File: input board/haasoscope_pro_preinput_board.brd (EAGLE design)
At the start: 75 x 50 mm, 20 parts, among them J1 MOLEX_BNC_73100-0105, J4 8pin, K1 AQY21SOP

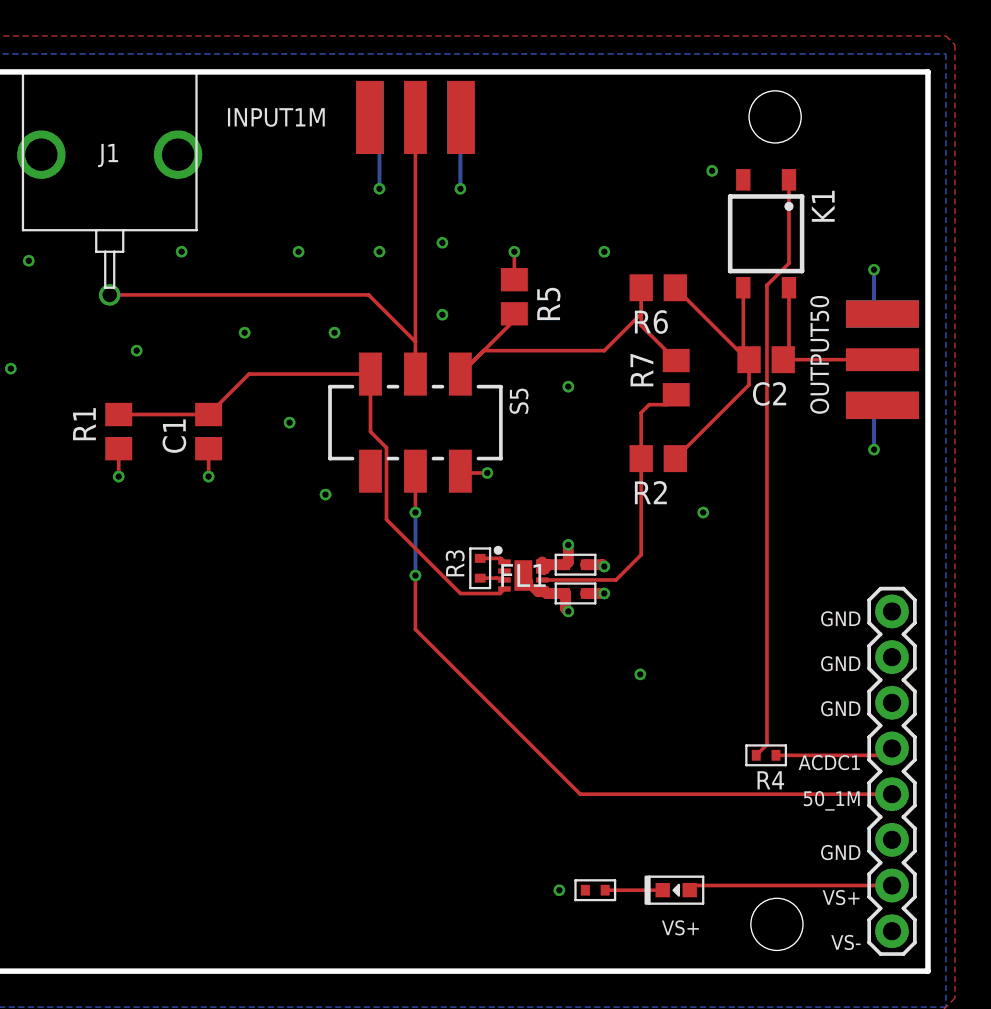
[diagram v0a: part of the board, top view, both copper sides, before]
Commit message: use rf relay instead of switch
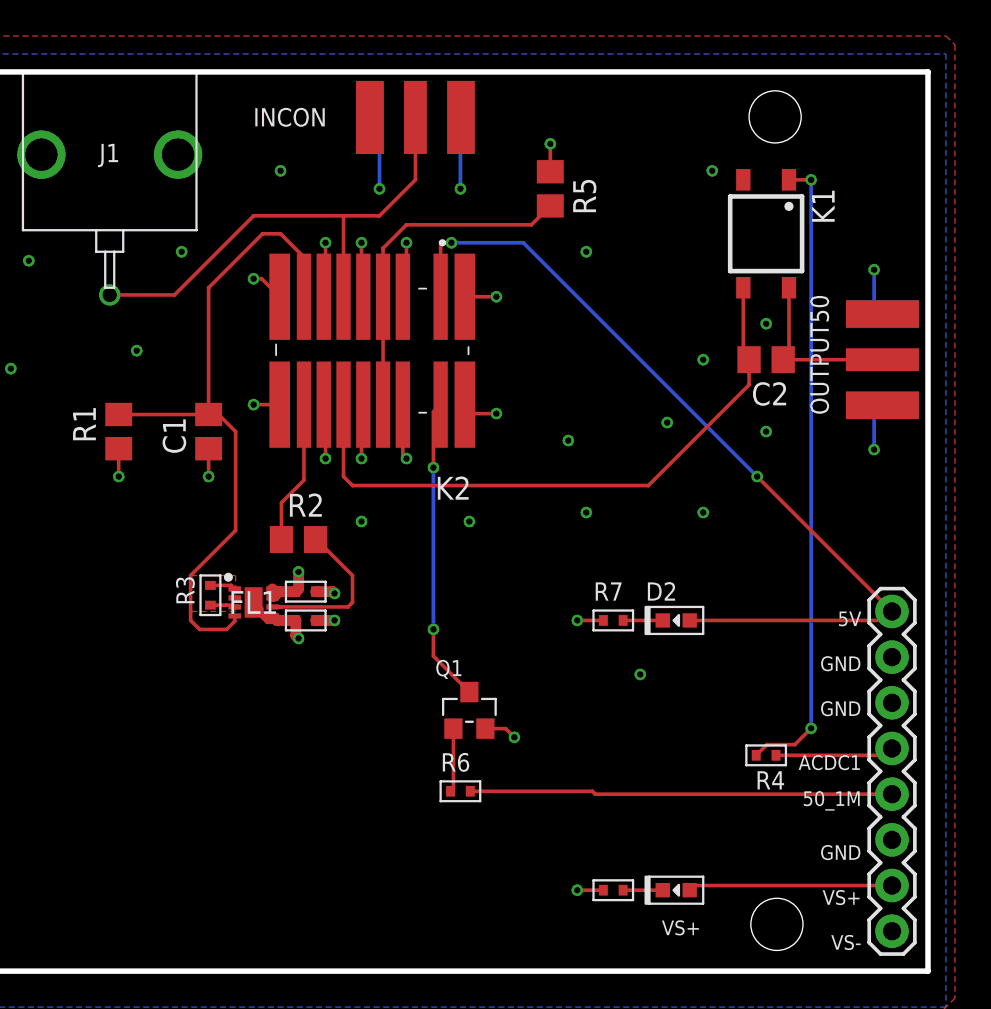
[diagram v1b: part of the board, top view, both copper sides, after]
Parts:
- removed S5: JS202011SCQN, switch-ck:JS202011SCQN
- added D2: green, MF_LEDs:LED0603
- added K2: G6K-2F-RF-T-TR03_DC5, G6K-2F-RF-T-TR03_DC5:G6K2FRFTTR03DC5
- added Q1: S8050, Seeed-Transistor:SOT-23
- INCON: value in1M -> in
- R6, R7: value 47 -> 1k; device resistor:R0805 -> MF_Passives:R0402
- moved R6 30.1 mm to (59.0, 10.0), turned to 0 degrees
- moved R2 20.5 mm to (50.0, 24.0), turned to 0 degrees
- moved C11 15.1 mm to (50.4, 21.1)
- moved C12 15.1 mm to (50.4, 19.5)
- moved FL1 15.1 mm to (47.5, 20.5)
- moved R3 15.1 mm to (45.1, 20.9)
- moved R7 13.9 mm to (67.5, 19.5), turned to 0 degrees
- moved R5 6.32 mm to (64.0, 43.5)
- moved R12 1.00 mm to (67.5, 4.50)
- renumbered INPUT1M to INCON
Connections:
- removed net N$10: C1.2, FL1.4, R1.2, S5.3
- removed net N$13: R5.2, R6.2, R7.2, S5.1
- removed net N$8: C2.2, K1.3, R2.1, R6.1
- new net 1MPATH: C1.2, FL1.4, K2.4, R1.2
- new net 1MPATH50: K2.5, R2.1
- new net 50PATH: K2.2, K2.7, R5.2
- new net 5V: D2.ANODE, J4.1, K2.1
- new net COIL1-: K2.8, Q1.3
- new net INPATH: INCON.P, J1.SIGNAL, K2.3
- new net N$7: D2.CATHODE, R7.P$2
- new net OUTPATH: C2.2, K1.3, K2.6
- net 50_1M: now also R6.P$2; no longer S5.5
- net GND: now also K2.MP1, K2.MP10, K2.MP2, K2.MP3, K2.MP4, K2.MP5, K2.MP6, K2.MP7, K2.MP8, K2.MP9, Q1.2, R7.P$1; no longer J4.1, S5.6
- net N$4: no longer R7.1
- net N$6: now also Q1.1, R6.P$1; no longer INCON.P, J1.SIGNAL, S5.2
- net VS+: no longer S5.4
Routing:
- net 5V: track 0.00 -> 48.0 mm, vias 0 -> 2
- net 1MPATH: track 0.00 -> 38.1 mm
- net OUTPATH: track 0.00 -> 35.1 mm
- net N$10: track 31.8 -> 0.00 mm
- net GND: track 20.3 -> 50.5 mm, vias 27 -> 39
- net N$6: track 32.3 -> 3.55 mm
- net INPATH: track 0.00 -> 27.6 mm
- net N$13: track 20.9 -> 0.00 mm
- net 50PATH: track 0.00 -> 20.5 mm
- net N$8: track 18.0 -> 0.00 mm
- net COIL1-: track 0.00 -> 17.0 mm, vias 0 -> 2
- net 50_1M: track 39.1 -> 23.5 mm, vias 2 -> 0
- net 1MPATH50: track 0.00 -> 8.37 mm
- net N$4: track 16.3 -> 9.43 mm
- net N$11: track 32.8 -> 35.4 mm, vias 0 -> 2
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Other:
- board text added: "5V"

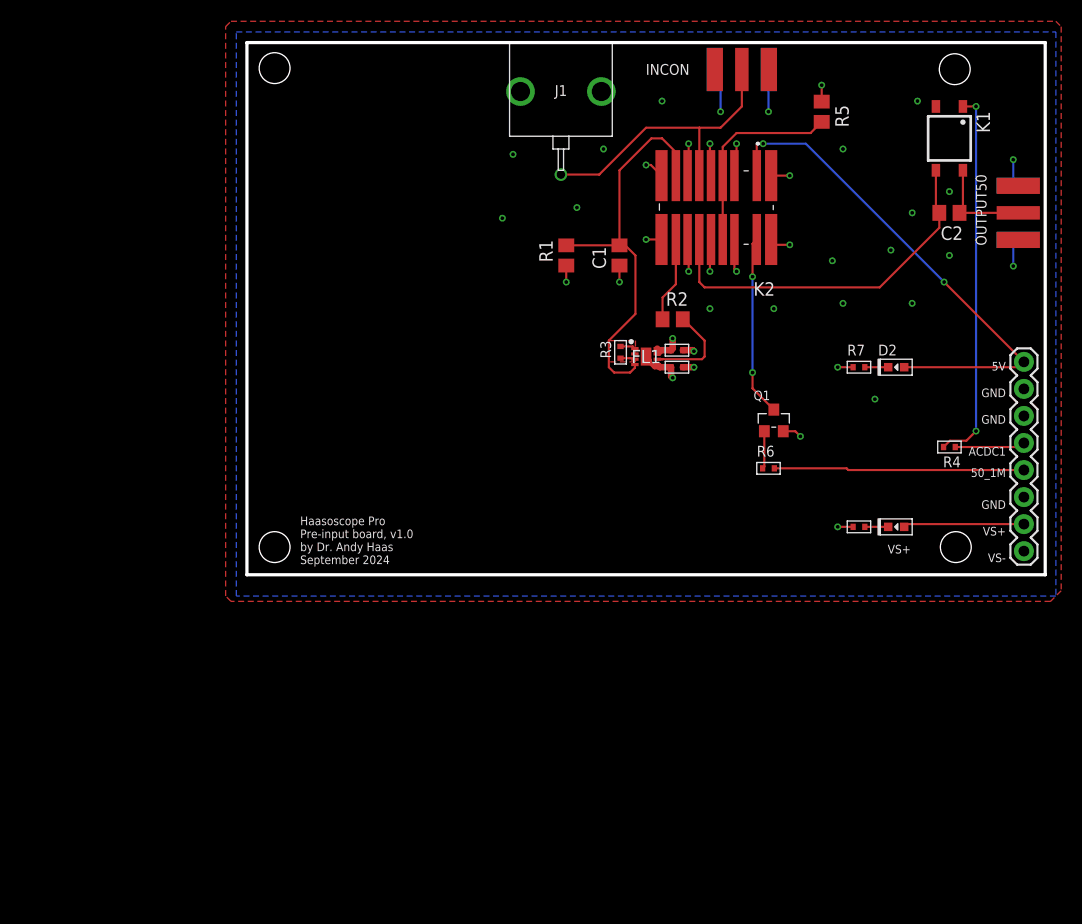
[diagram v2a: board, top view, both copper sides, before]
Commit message: add attenuator and fix relay footprint
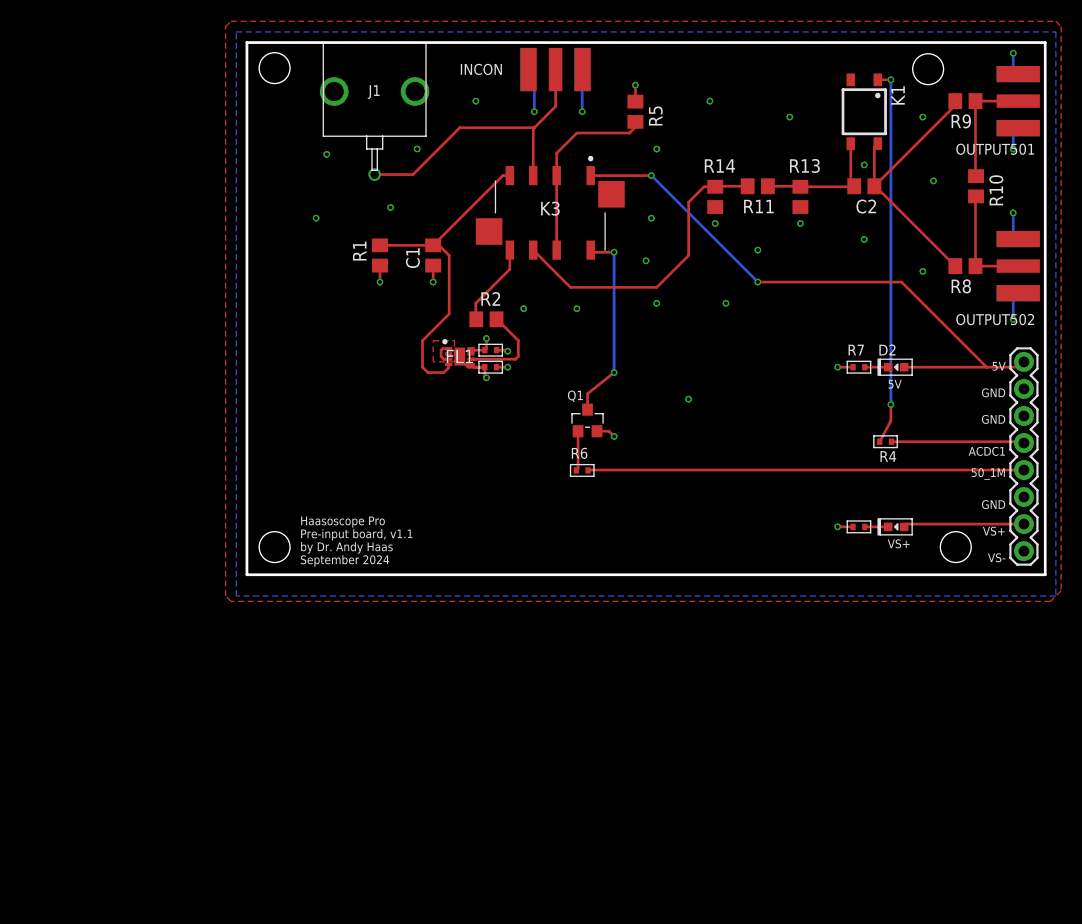
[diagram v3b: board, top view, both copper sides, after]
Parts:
- removed K2: G6K-2F-RF-T-TR03_DC5, G6K-2F-RF-T-TR03_DC5:G6K2FRFTTR03DC5
- removed OUTPUT50: out50, adafruit:SMA_EDGELAUNCH
- removed R3: 0, MF_Passives:R0402
- added K3: G6K-2F-RF-DC3, G6K-2F-RF-DC3:G6K2FRFDC3
- added OUTPUT501, OUTPUT502: out50, adafruit:SMA_EDGELAUNCH
- added R10, R8, R9: 47, resistor:R0805
- added R11: 120, resistor:R0805
- added R13, R14: 75, resistor:R0805
- R5: value 47 -> ?50?
- moved R6 17.5 mm to (41.5, 9.80)
- moved C1 17.5 mm to (27.5, 30.0)
- moved C11 17.5 mm to (32.9, 21.1)
- moved C12 17.5 mm to (32.9, 19.5)
- moved FL1 17.5 mm to (30.0, 20.5)
- moved INCON 17.5 mm to (39.0, 49.5)
- moved J1 17.5 mm to (22.0, 41.5)
- moved Q1 17.5 mm to (42.0, 14.5)
- moved R1 17.5 mm to (22.5, 30.0)
- moved R2 17.5 mm to (32.5, 24.0)
- moved R5 17.5 mm to (46.5, 43.5)
- moved C2 8.38 mm to (68.0, 36.5)
- moved K1 8.38 mm to (68.0, 43.5)
- moved R4 6.02 mm to (70.0, 12.5)
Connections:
- removed net N$2: FL1.3, R3.P$2
- removed net N$3: C2.1, K1.4, OUTPUT50.P
- new net N$10: OUTPUT501.P, R10.1, R9.1
- new net N$8: C2.1, K1.4, R8.2, R9.2
- new net N$9: OUTPUT502.P, R10.2, R8.1
- new net OUTPATHFILT: C2.2, K1.3, R11.1, R13.1
- net 1MPATH: now also K3.4; no longer K2.4
- net 1MPATH50: now also K3.5; no longer K2.5
- net 50PATH: now also K3.2, K3.7; no longer K2.2, K2.7
- net 5V: now also K3.1; no longer K2.1
- net COIL1-: now also K3.8; no longer K2.8
- net GND: now also K3.MP1, K3.MP2, OUTPUT501.GND@1, OUTPUT501.GND@2, OUTPUT501.GND@3, OUTPUT501.GND@4, OUTPUT502.GND@1, OUTPUT502.GND@2, OUTPUT502.GND@3, OUTPUT502.GND@4, R13.2, R14.2; no longer K2.MP1, K2.MP10, K2.MP2, K2.MP3, K2.MP4, K2.MP5, K2.MP6, K2.MP7, K2.MP8, K2.MP9, OUTPUT50.GND@1, OUTPUT50.GND@2, OUTPUT50.GND@3, OUTPUT50.GND@4
- net INPATH: now also K3.3; no longer K2.3
- net N$5: now also FL1.3; no longer R3.P$1
- net OUTPATH: now also K3.6, R11.2, R14.1; no longer C2.2, K1.3, K2.6
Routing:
- net N$8: track 0.00 -> 26.4 mm
- net GND: track 50.5 -> 29.6 mm, vias 39 -> 37
- net 50_1M: track 23.5 -> 41.0 mm
- net OUTPATHFILT: track 0.00 -> 12.8 mm
- net N$10: track 0.00 -> 12.0 mm
- net N$9: track 0.00 -> 11.1 mm
- net N$3: track 9.65 -> 0.00 mm
- net 5V: track 48.0 -> 56.1 mm
- net OUTPATH: track 35.1 -> 28.5 mm
- net 1MPATH: track 38.1 -> 31.5 mm
- net ACDC1: track 6.61 -> 12.5 mm
- net 50PATH: track 20.5 -> 18.4 mm
- net COIL1-: track 17.0 -> 18.4 mm
- net N$2: track 1.39 -> 0.00 mm
- net N$5: track 1.43 -> 2.19 mm
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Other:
- board text added: "Haasoscope Pro Pre-input board, v1.1 by Dr. Andy Haas September 2024"
- board text removed: "Haasoscope Pro Pre-input board, v1.0 by Dr. Andy Haas September 2024"

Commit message: add relay for attenuator
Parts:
- added K2: G6K-2F-RF-DC3, G6K-2F-RF-DC3:G6K2FRFDC3
- added Q2: S8050, Seeed-Transistor:SOT-23
- added R3: 1k, MF_Passives:R0402
- moved R11 10.6 mm to (54.5, 46.5)
- moved R14 9.86 mm to (49.0, 44.0)
- moved R13 9.01 mm to (59.0, 44.0)
- moved C1 6.50 mm to (21.0, 30.0)
- moved C11 6.50 mm to (26.4, 21.1)
- moved C12 6.50 mm to (26.4, 19.5)
- moved FL1 6.50 mm to (23.5, 20.5)
- moved INCON 6.50 mm to (32.5, 49.5)
- moved J1 6.50 mm to (15.5, 41.5)
- moved K3 6.50 mm to (32.0, 34.0)
- moved Q1 6.50 mm to (35.5, 14.5)
- moved R1 6.50 mm to (16.0, 30.0)
- moved R2 6.50 mm to (26.0, 24.0)
- moved R5 6.50 mm to (40.0, 43.5)
- moved R6 6.50 mm to (35.0, 9.80)
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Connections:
- new net ATT: J4.3, R3.P$2
- new net COIL2-: K2.8, Q2.3
- new net FILTIN: K2.4, R11.2, R14.1
- new net FILTOUT: K2.5, R11.1, R13.1
- new net N$2: Q2.1, R3.P$1
- new net NOFILT: K2.2, K2.7
- net 5V: now also K2.1
- net GND: now also K2.MP1, K2.MP2, Q2.2; no longer J4.3
- net OUTPATH: now also K2.3; no longer R11.2, R14.1
- net OUTPATHFILT: now also K2.6; no longer R11.1, R13.1
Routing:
- net ATT: track 0.00 -> 32.8 mm
- net COIL2-: track 0.00 -> 27.1 mm, vias 0 -> 2
- net FILTIN: track 0.00 -> 21.5 mm
- net 5V: track 56.1 -> 74.7 mm
- net FILTOUT: track 0.00 -> 12.0 mm
- net OUTPATHFILT: track 12.8 -> 21.8 mm
- net NOFILT: track 0.00 -> 7.00 mm
- net 50_1M: track 41.0 -> 47.5 mm
- net N$2: track 0.00 -> 6.13 mm
- net OUTPATH: track 28.5 -> 26.7 mm
- net N$11: track 35.5 -> 36.4 mm
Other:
- board text added: "ATT"
- board text added: "Haasoscope Pro Pre-input board, v1.11 by Dr. Andy Haas September 2024"
- board text removed: "Haasoscope Pro Pre-input board, v1.1 by Dr. Andy Haas September 2024"

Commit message: don't place 10pF, fix some labels
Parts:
- C1: value 10pF -> ?10pF?
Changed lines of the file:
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@@
 <element name="R1" library="resistor" library_urn="urn:adsk.eagle:library:348" package="R0805" package3d_urn="urn:adsk.eagle:package:23553/2" value="1M" x="16" y="30" smashed="yes" rot="R90">
 <attribute name="NAME" x="14.73" y="29.365" size="1.27" layer="25" rot="R90"/>
-<attribute name="VALUE" x="18.54" y="29.365" size="1.27" layer="27" rot="R90"/>
+<attribute name="VALUE" x="18.44" y="29.065" size="1.27" layer="21" rot="R90"/>
 </element>
-<element name="C1" library="resistor" library_urn="urn:adsk.eagle:library:348" package="C0805" package3d_urn="urn:adsk.eagle:package:23617/2" value="10pF" x="21" y="30" smashed="yes" rot="R90">
-<attribute name="NAME" x="19.73" y="28.73" size="1.27" layer="25" rot="R90"/>
-<attribute name="VALUE" x="23.54" y="28.73" size="1.27" layer="27" rot="R90"/>
+<element name="C1" library="resistor" library_urn="urn:adsk.eagle:library:348" package="C0805" package3d_urn="urn:adsk.eagle:package:23617/2" value="?10pF?" x="21" y="30" smashed="yes" rot="R90">
+<attribute name="NAME" x="19.83" y="29.13" size="1.27" layer="25" rot="R90"/>
+<attribute name="VALUE" x="23.54" y="27.73" size="1.27" layer="21" rot="R90"/>
 </element>
 <element name="R2" library="resistor" library_urn="urn:adsk.eagle:library:348" package="R0805" package3d_urn="urn:adsk.eagle:package:23553/2" value="47" x="26" y="24" smashed="yes">
 <attribute name="NAME" x="25.365" y="25.27" size="1.27" layer="25"/>
-<attribute name="VALUE" x="25.365" y="21.46" size="1.27" layer="27"/>
+<attribute name="VALUE" x="25.265" y="21.86" size="1.27" layer="21"/>
 </element>
 <element name="J1" library="connector" package="MOLEX-BNC-73100-0105" value="MOLEX_BNC_73100-0105" x="15.5" y="41.5" smashed="yes" rot="R180">
@@
 <element name="C2" library="resistor" library_urn="urn:adsk.eagle:library:348" package="C0805" package3d_urn="urn:adsk.eagle:package:23617/2" value="1uF" x="68" y="36.5" smashed="yes" rot="R180">
 <attribute name="NAME" x="69.27" y="35.23" size="1.27" layer="25" rot="R180"/>
-<attribute name="VALUE" x="69.27" y="39.04" size="1.27" layer="27" rot="R180"/>
+<attribute name="VALUE" x="69.27" y="39.04" size="1.27" layer="21" rot="R180"/>
 </element>
 <element name="R5" library="resistor" library_urn="urn:adsk.eagle:library:348" package="R0805" package3d_urn="urn:adsk.eagle:package:23553/2" value="?50?" x="40" y="43.5" smashed="yes" rot="R270">
 <attribute name="NAME" x="41.27" y="44.135" size="1.27" layer="25" rot="R270"/>
-<attribute name="VALUE" x="37.46" y="44.135" size="1.27" layer="27" rot="R270"/>
+<attribute name="VALUE" x="37.46" y="45.135" size="1.27" layer="21" rot="R270"/>
 </element>
 <element name="Q1" library="Seeed-Transistor" library_urn="urn:adsk.eagle:library:477" package="SOT-23" package3d_urn="urn:adsk.eagle:package:33015/1" value="S8050" x="35.5" y="14.5" smashed="yes">
@@
 <attribute name="MOUSER_PRICE-STOCK" value="https://www.mouser.co.uk/ProductDetail/Omron-Electronics/G6K-2F-RF-DC3?qs=Pjd0UV7BHP8BL6Nr%252BzW3GA%3D%3D" x="32" y="34" size="1.778" layer="27" rot="R180" display="off"/>
 <attribute name="NAME" x="32" y="34.4" size="1.27" layer="25" rot="R180" align="center"/>
-<attribute name="VALUE" x="32" y="27.9" size="1.27" layer="27" rot="R180" align="center"/>
+<attribute name="VALUE" x="32" y="27.9" size="1.27" layer="21" rot="R180" align="center"/>
 </element>
 <element name="OUTPUT501" library="adafruit" package="SMA_EDGELAUNCH" value="out50" x="84.5" y="44.5" smashed="yes" rot="R180">
@@
 <element name="R8" library="resistor" library_urn="urn:adsk.eagle:library:348" package="R0805" package3d_urn="urn:adsk.eagle:package:23553/2" value="47" x="77.5" y="29" smashed="yes" rot="R180">
 <attribute name="NAME" x="78.135" y="27.73" size="1.27" layer="25" rot="R180"/>
-<attribute name="VALUE" x="78.135" y="31.54" size="1.27" layer="27" rot="R180"/>
+<attribute name="VALUE" x="78.135" y="31.54" size="1.27" layer="21" rot="R180"/>
 </element>
 <element name="R9" library="resistor" library_urn="urn:adsk.eagle:library:348" package="R0805" package3d_urn="urn:adsk.eagle:package:23553/2" value="47" x="77.5" y="44.5" smashed="yes" rot="R180">
 <attribute name="NAME" x="78.135" y="43.23" size="1.27" layer="25" rot="R180"/>
-<attribute name="VALUE" x="78.135" y="47.04" size="1.27" layer="27" rot="R180"/>
+<attribute name="VALUE" x="78.135" y="47.04" size="1.27" layer="21" rot="R180"/>
 </element>
 <element name="R10" library="resistor" library_urn="urn:adsk.eagle:library:348" package="R0805" package3d_urn="urn:adsk.eagle:package:23553/2" value="47" x="78.5" y="36.5" smashed="yes" rot="R270">
 <attribute name="NAME" x="79.77" y="37.635" size="1.27" layer="25" rot="R270"/>
-<attribute name="VALUE" x="75.96" y="37.135" size="1.27" layer="27" rot="R270"/>
+<attribute name="VALUE" x="75.96" y="37.135" size="1.27" layer="21" rot="R270"/>
 </element>
 <element name="Q2" library="Seeed-Transistor" library_urn="urn:adsk.eagle:library:477" package="SOT-23" package3d_urn="urn:adsk.eagle:package:33015/1" value="S8050" x="47.5" y="14.5" smashed="yes">
@@
 <attribute name="MOUSER_PRICE-STOCK" value="https://www.mouser.co.uk/ProductDetail/Omron-Electronics/G6K-2F-RF-DC3?qs=Pjd0UV7BHP8BL6Nr%252BzW3GA%3D%3D" x="47" y="31.5" size="1.778" layer="27" display="off"/>
 <attribute name="NAME" x="52" y="34.6" size="1.27" layer="25" align="center"/>
-<attribute name="VALUE" x="52" y="28.1" size="1.27" layer="27" align="center"/>
+<attribute name="VALUE" x="52" y="28.1" size="1.27" layer="21" align="center"/>
 </element>
 <element name="R11" library="resistor" library_urn="urn:adsk.eagle:library:348" package="R0805" package3d_urn="urn:adsk.eagle:package:23553/2" value="120" x="54.5" y="46.5" smashed="yes" rot="R180">
 <attribute name="NAME" x="56.135" y="45.23" size="1.27" layer="25" rot="R180"/>
-<attribute name="VALUE" x="55.135" y="49.04" size="1.27" layer="27" rot="R180"/>
+<attribute name="VALUE" x="55.135" y="49.04" size="1.27" layer="21" rot="R180"/>
 </element>
 <element name="R13" library="resistor" library_urn="urn:adsk.eagle:library:348" package="R0805" package3d_urn="urn:adsk.eagle:package:23553/2" value="75" x="59" y="44" smashed="yes" rot="R270">
 <attribute name="LCSC" value="C113304" x="59" y="44" size="1.778" layer="27" rot="R270" display="off"/>
 <attribute name="NAME" x="60.27" y="45.635" size="1.27" layer="25" rot="R270"/>
-<attribute name="VALUE" x="56.46" y="44.635" size="1.27" layer="27" rot="R270"/>
+<attribute name="VALUE" x="56.46" y="44.635" size="1.27" layer="21" rot="R270"/>
 </element>
 <element name="R14" library="resistor" library_urn="urn:adsk.eagle:library:348" package="R0805" package3d_urn="urn:adsk.eagle:package:23553/2" value="75" x="49" y="44" smashed="yes" rot="R270">
 <attribute name="LCSC" value="C113304" x="49" y="44" size="1.778" layer="27" rot="R270" display="off"/>
 <attribute name="NAME" x="50.27" y="45.635" size="1.27" layer="25" rot="R270"/>
-<attribute name="VALUE" x="46.46" y="44.635" size="1.27" layer="27" rot="R270"/>
+<attribute name="VALUE" x="46.46" y="44.635" size="1.27" layer="21" rot="R270"/>
 </element>
 </elements>
